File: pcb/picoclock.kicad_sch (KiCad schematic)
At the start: 62 parts, among them J1 UART, J10 USB, J11 Alt Power, J2 AUDIO, J3 xx, J4 xx, J5 Power In, J6 USB_C_Receptacle, J7 xx, J8 xx, J9 screen_adapter_connector, SW1 SW_Push, SW2 SW_Push, SW3 SW_Push, SW4 SW_Push, SW5 SW_Push, SW6 SW_Push, U1 PCF8563T, U2 Pico, U3 MCP9808_MSOP, U4 PCM5100, Y1 Crystal

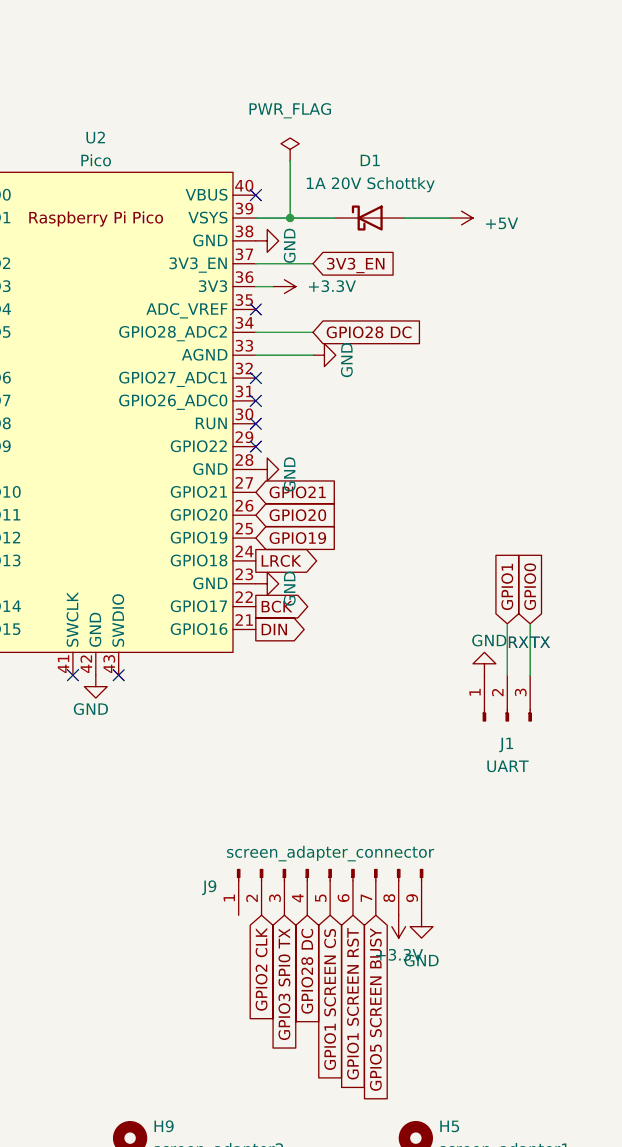
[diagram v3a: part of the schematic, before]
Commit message: [pcb] add PWR from epaper hat
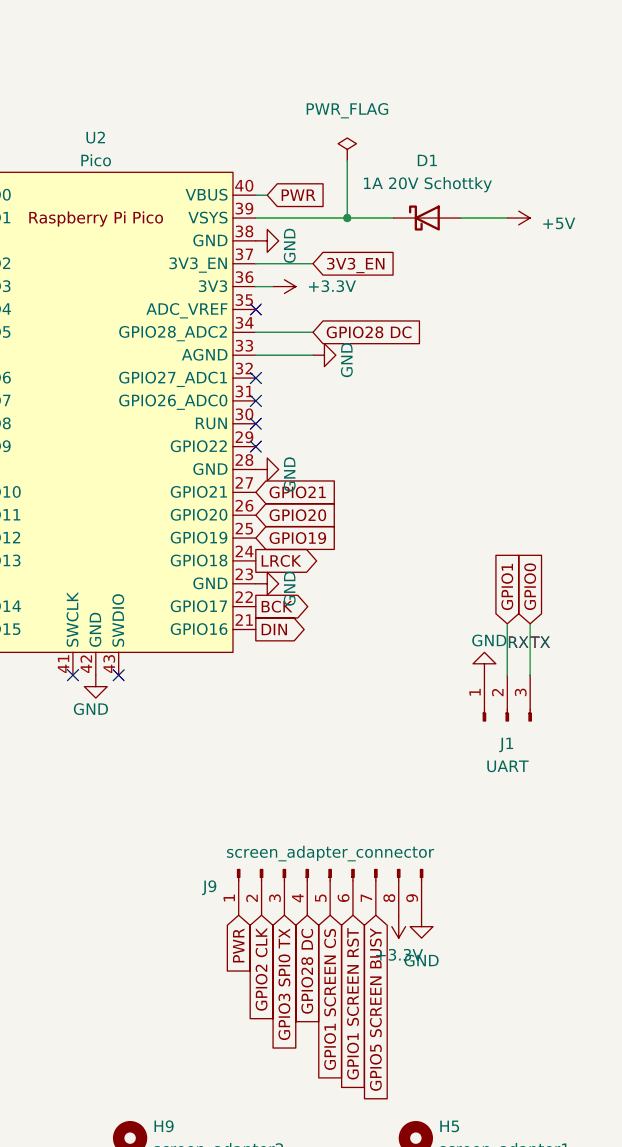
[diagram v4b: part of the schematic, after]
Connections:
- net PWR: now reaches J9.1 (Pin_1)
- net PWR: now also U2.40 (VBUS)
- no-connect marks 10 -> 9
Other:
- moved on the sheet: D1
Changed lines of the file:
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@@
   (junction (at 136.525 115.57) (diameter 0) (color 0 0 0 0)
   )
-  (junction (at 243.84 40.64) (diameter 0) (color 0 0 0 0)
-  )
   (junction (at 46.99 161.29) (diameter 0) (color 0 0 0 0)
   )
@@
   (junction (at 107.95 160.02) (diameter 0) (color 0 0 0 0)
   )
+  (junction (at 250.19 40.64) (diameter 0) (color 0 0 0 0)
+  )
   (junction (at 37.465 171.45) (diameter 0) (color 0 0 0 0)
   )
@@
   (no_connect (at 240.03 50.8))
   (no_connect (at 240.03 63.5))
-  (no_connect (at 240.03 38.1))
   (no_connect (at 204.47 86.36))
   (no_connect (at 240.03 60.96))
@@
     (stroke (width 0) (type default))
   )
-  (wire (pts (xy 256.54 40.64) (xy 261.62 40.64))
+  (wire (pts (xy 262.89 40.64) (xy 267.97 40.64))
     (stroke (width 0) (type default))
   )
@@
     (stroke (width 0) (type default))
   )
+  (wire (pts (xy 240.03 40.64) (xy 250.19 40.64))
+    (stroke (width 0) (type default))
+  )
   (polyline (pts (xy 15.875 148.59) (xy 15.875 192.405))
     (stroke (width 0) (type default))
@@
     (stroke (width 0) (type default))
   )
+  (wire (pts (xy 240.03 38.1) (xy 241.3 38.1))
+    (stroke (width 0) (type default))
+  )
   (wire (pts (xy 100.33 58.42) (xy 100.33 62.865))
     (stroke (width 0) (type default))
@@
     (stroke (width 0) (type default))
   )
-  (wire (pts (xy 243.84 34.29) (xy 243.84 40.64))
+  (wire (pts (xy 250.19 34.29) (xy 250.19 40.64))
     (stroke (width 0) (type default))
   )
@@
     (stroke (width 0) (type default))
   )
+  (wire (pts (xy 250.19 40.64) (xy 255.27 40.64))
+    (stroke (width 0) (type default))
+  )
   (wire (pts (xy 45.085 132.715) (xy 45.085 137.795))
     (stroke (width 0) (type default))
@@
     (stroke (width 0) (type default))
   )
-  (wire (pts (xy 243.84 40.64) (xy 248.92 40.64))
-    (stroke (width 0) (type default))
-  )
   (wire (pts (xy 33.02 171.45) (xy 37.465 171.45))
     (stroke (width 0) (type default))
@@
     (stroke (width 0) (type default))
   )
-  (wire (pts (xy 240.03 40.64) (xy 243.84 40.64))
-    (stroke (width 0) (type default))
-  )
   (text "Internal Temperature" (at 17.78 144.78 0)
     (effects (font (size 1.27 1.27)) (justify left bottom))
@@
     )
   )
+  (global_label "PWR" (shape input) (at 241.3 38.1 0) (fields_autoplaced)
+    (effects (font (size 1.27 1.27)) (justify left))
+    (property "Intersheetrefs" "${INTERSHEET_REFS}" (at 248.2766 38.1 0)
+      (effects (font (size 1.27 1.27)) (justify left) hide)
+    )
+  )
   (global_label "GPIO11" (shape input) (at 158.75 33.655 270) (fields_autoplaced)
     (effects (font (size 1.27 1.27)) (justify right))
@@
     )
   )
+  (global_label "PWR" (shape input) (at 238.125 118.11 270) (fields_autoplaced)
+    (effects (font (size 1.27 1.27)) (justify right))
+    (property "Intersheetrefs" "${INTERSHEET_REFS}" (at 238.125 125.0866 90)
+      (effects (font (size 1.27 1.27)) (justify right) hide)
+    )
+  )
   (global_label "GPIO21" (shape input) (at 107.315 104.14 0) (fields_autoplaced)
     (effects (font (size 1.27 1.27)) (justify left))
@@
     )
   )
-  (symbol (lib_id "power:+5V") (at 261.62 40.64 270) (unit 1)
+  (symbol (lib_id "power:+5V") (at 267.97 40.64 270) (unit 1)
     (in_bom yes) (on_board yes) (dnp no) (fields_autoplaced)
-    (property "Reference" "#PWR017" (at 257.81 40.64 0)
+    (property "Reference" "#PWR017" (at 264.16 40.64 0)
       (effects (font (size 1.27 1.27)) hide)
     )
-    (property "Value" "+5V" (at 265.43 41.275 90)
+    (property "Value" "+5V" (at 271.78 41.275 90)
       (effects (font (size 1.27 1.27)) (justify left))
     )
-    (property "Footprint" "" (at 261.62 40.64 0)
+    (property "Footprint" "" (at 267.97 40.64 0)
       (effects (font (size 1.27 1.27)) hide)
     )
-    (property "Datasheet" "" (at 261.62 40.64 0)
+    (property "Datasheet" "" (at 267.97 40.64 0)
       (effects (font (size 1.27 1.27)) hide)
     )
@@
     )
   )
-  (symbol (lib_id "Device:D_Schottky") (at 252.73 40.64 0) (unit 1)
+  (symbol (lib_id "Device:D_Schottky") (at 259.08 40.64 0) (unit 1)
     (in_bom yes) (on_board yes) (dnp no)
-    (property "Reference" "D1" (at 252.73 34.29 0)
+    (property "Reference" "D1" (at 259.08 34.29 0)
       (effects (font (size 1.27 1.27)))
     )
-    (property "Value" "1A 20V Schottky" (at 252.73 36.83 0)
+    (property "Value" "1A 20V Schottky" (at 259.08 36.83 0)
       (effects (font (size 1.27 1.27)))
     )
-    (property "Footprint" "Diode_SMD:D_SOD-123F" (at 252.73 40.64 0)
+    (property "Footprint" "Diode_SMD:D_SOD-123F" (at 259.08 40.64 0)
       (effects (font (size 1.27 1.27)) hide)
     )
-    (property "Datasheet" "~" (at 252.73 40.64 0)
+    (property "Datasheet" "~" (at 259.08 40.64 0)
       (effects (font (size 1.27 1.27)) hide)
     )
-    (property "LCSC" "C169527" (at 252.73 40.64 0)
+    (property "LCSC" "C169527" (at 259.08 40.64 0)
       (effects (font (size 1.27 1.27)) hide)
     )
@@
     )
   )
-  (symbol (lib_id "power:PWR_FLAG") (at 243.84 34.29 0) (unit 1)
+  (symbol (lib_id "power:PWR_FLAG") (at 250.19 34.29 0) (unit 1)
     (in_bom yes) (on_board yes) (dnp no) (fields_autoplaced)
-    (property "Reference" "#FLG01" (at 243.84 32.385 0)
+    (property "Reference" "#FLG01" (at 250.19 32.385 0)
       (effects (font (size 1.27 1.27)) hide)
     )
-    (property "Value" "PWR_FLAG" (at 243.84 28.575 0)
+    (property "Value" "PWR_FLAG" (at 250.19 28.575 0)
       (effects (font (size 1.27 1.27)))
     )
-    (property "Footprint" "" (at 243.84 34.29 0)
+    (property "Footprint" "" (at 250.19 34.29 0)
       (effects (font (size 1.27 1.27)) hide)
     )
-    (property "Datasheet" "~" (at 243.84 34.29 0)
+    (property "Datasheet" "~" (at 250.19 34.29 0)
       (effects (font (size 1.27 1.27)) hide)
     )

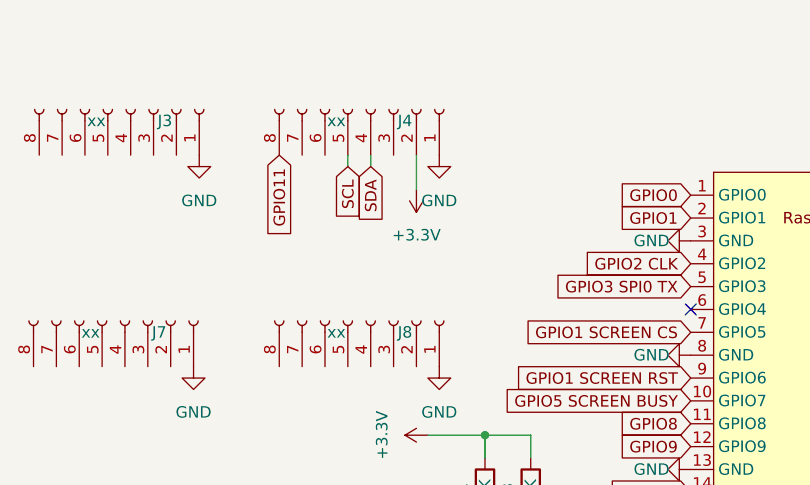
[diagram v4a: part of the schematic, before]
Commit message: [pcb] fix frontpanel pcb LEDs + connexion to main pcb
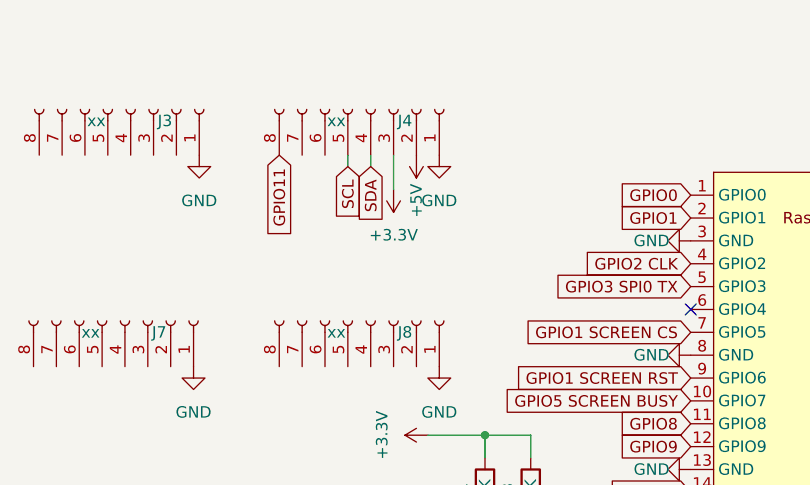
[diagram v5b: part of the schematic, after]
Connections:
- net +3.3V: now also J4.3 (Pin_3); no longer J4.2 (Pin_2)
- net +5V: now also J4.2 (Pin_2)
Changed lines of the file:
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@@
-    (stroke (width 0) (type default))
-  )
-  (wire (pts (xy 173.99 37.465) (xy 173.99 33.655))
     (stroke (width 0) (type default))
   )
@@
   )
   (wire (pts (xy 50.8 161.29) (xy 73.025 161.29))
+    (stroke (width 0) (type default))
+  )
+  (wire (pts (xy 171.45 37.465) (xy 171.45 33.655))
     (stroke (width 0) (type default))
   )
@@
     )
   )
+  (symbol (lib_id "power:+3.3V") (at 171.45 37.465 180) (unit 1)
+    (in_bom yes) (on_board yes) (dnp no)
+    (property "Reference" "#PWR048" (at 171.45 33.655 0)
+      (effects (font (size 1.27 1.27)) hide)
+    )
+    (property "Value" "+3.3V" (at 171.45 42.545 0)
+      (effects (font (size 1.27 1.27)))
+    )
+    (property "Footprint" "" (at 171.45 37.465 0)
+      (effects (font (size 1.27 1.27)) hide)
+    )
+    (property "Datasheet" "" (at 171.45 37.465 0)
+      (effects (font (size 1.27 1.27)) hide)
+    )
+    (pin "1")
+    (instances
+      (project "picoclock"
+        (path "/3b9dec0e-e0b7-4565-afc9-c4692f41aea9"
+          (reference "#PWR048") (unit 1)
+        )
+      )
+    )
+  )
   (symbol (lib_id "power:+3.3V") (at 136.525 120.015 270) (unit 1)
     (in_bom yes) (on_board yes) (dnp no)
@@
     )
   )
-  (symbol (lib_id "power:+3.3V") (at 173.99 37.465 180) (unit 1)
-    (in_bom yes) (on_board yes) (dnp no)
-    (property "Reference" "#PWR048" (at 173.99 33.655 0)
-      (effects (font (size 1.27 1.27)) hide)
-    )
-    (property "Value" "+3.3V" (at 173.99 42.545 0)
-      (effects (font (size 1.27 1.27)))
-    )
-    (property "Footprint" "" (at 173.99 37.465 0)
-      (effects (font (size 1.27 1.27)) hide)
-    )
-    (property "Datasheet" "" (at 173.99 37.465 0)
-      (effects (font (size 1.27 1.27)) hide)
-    )
-    (pin "1")
-    (instances
-      (project "picoclock"
-        (path "/3b9dec0e-e0b7-4565-afc9-c4692f41aea9"
-          (reference "#PWR048") (unit 1)
-        )
-      )
-    )
-  )
   (symbol (lib_id "power:+3.3V") (at 105.41 107.95 270) (unit 1)
     (in_bom yes) (on_board yes) (dnp no)
@@
         )
       )
+    )
+  )
+  (symbol (lib_id "power:+5V") (at 173.99 33.655 180) (unit 1)
+    (in_bom yes) (on_board yes) (dnp no)
+    (property "Reference" "#PWR070" (at 173.99 29.845 0)
+      (effects (font (size 1.27 1.27)) hide)
+    )
+    (property "Value" "+5V" (at 173.99 36.83 90)
+      (effects (font (size 1.27 1.27)) (justify left))
+    )
+    (property "Footprint" "" (at 173.99 33.655 0)
+      (effects (font (size 1.27 1.27)) hide)
+    )
+    (property "Datasheet" "" (at 173.99 33.655 0)
+      (effects (font (size 1.27 1.27)) hide)
+    )
+    (pin "1")
+    (instances
+      (project "picoclock"
+        (path "/3b9dec0e-e0b7-4565-afc9-c4692f41aea9"
+          (reference "#PWR070") (unit 1)
+        )
+      )

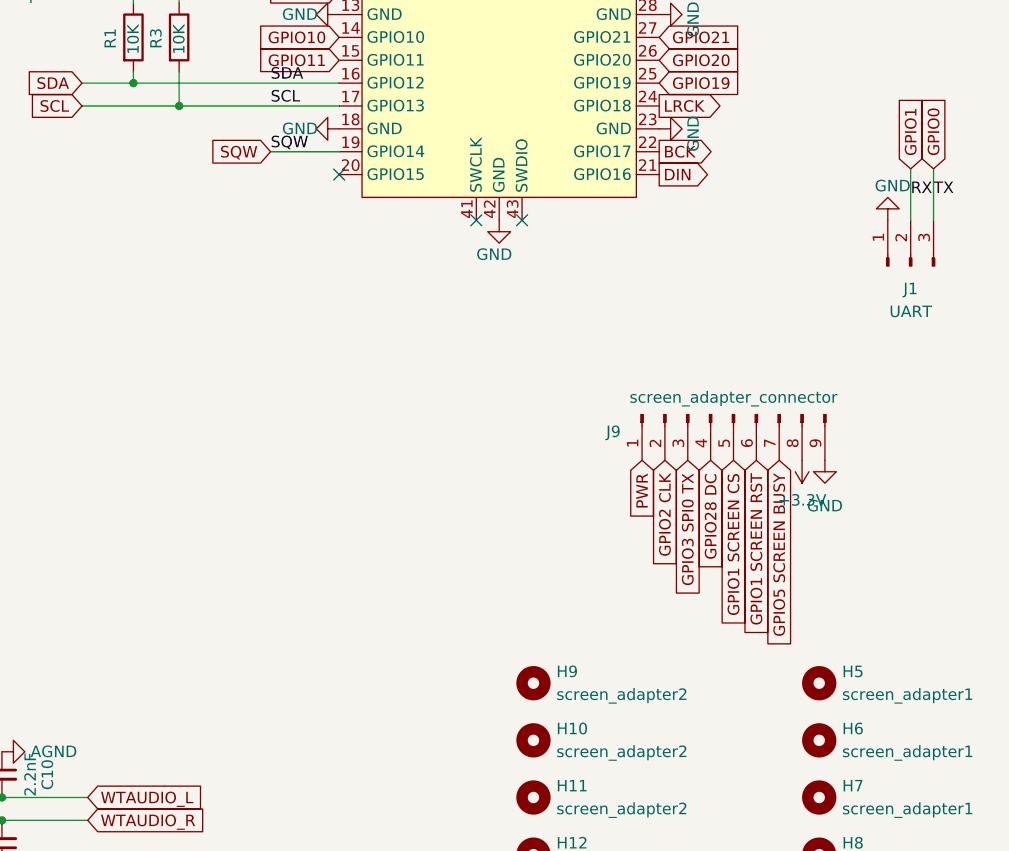
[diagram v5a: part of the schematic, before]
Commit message: [pcb] add PWM out
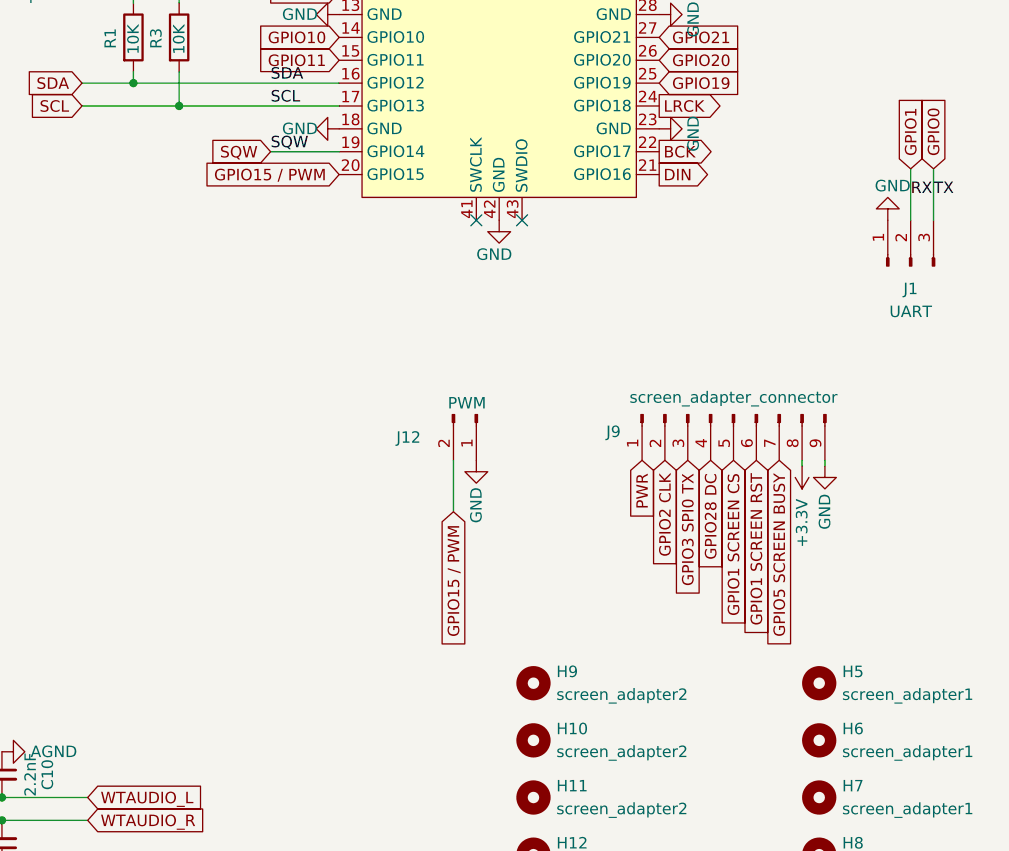
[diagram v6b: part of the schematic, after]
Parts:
- added J12: PWM, Connector_PinHeader_2.54mm:PinHeader_1x02_P2.54mm_Vertical, symbol Connector:Conn_01x02_Pin
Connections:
- net GND: now also J12.1 (Pin_1)
- net GPIO15 / PWM: now reaches U2.20 (GPIO15)
- net GPIO15 / PWM: now also J12.2 (Pin_2)
- no-connect marks 9 -> 8
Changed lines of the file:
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@@
   (no_connect (at 240.03 50.8))
   (no_connect (at 240.03 63.5))
-  (no_connect (at 204.47 86.36))
   (no_connect (at 240.03 60.96))
   (no_connect (at 204.47 50.8))
@@
     (stroke (width 0) (type default))
   )
+  (wire (pts (xy 217.17 123.825) (xy 217.17 118.11))
+    (stroke (width 0) (type default))
+  )
   (polyline (pts (xy 15.875 192.405) (xy 87.63 192.405))
     (stroke (width 0) (type default))
@@
     (stroke (width 0) (type default))
   )
+  (wire (pts (xy 255.905 118.745) (xy 255.905 118.11))
+    (stroke (width 0) (type default))
+  )
   (wire (pts (xy 33.02 48.26) (xy 35.56 48.26))
     (stroke (width 0) (type default))
@@
     (stroke (width 0) (type default))
   )
+  (wire (pts (xy 258.445 118.745) (xy 258.445 118.11))
+    (stroke (width 0) (type default))
+  )
   (wire (pts (xy 105.41 47.625) (xy 105.41 56.515))
     (stroke (width 0) (type default))
@@
     )
   )
+  (global_label "GPIO15 {slash} PWM" (shape input) (at 204.47 86.36 180) (fields_autoplaced)
+    (effects (font (size 1.27 1.27)) (justify right))
+    (property "Intersheetrefs" "${INTERSHEET_REFS}" (at 187.152 86.36 0)
+      (effects (font (size 1.27 1.27)) (justify right) hide)
+    )
+  )
   (global_label "GPIO0" (shape input) (at 204.47 38.1 180) (fields_autoplaced)
     (effects (font (size 1.27 1.27)) (justify right))
@@
     )
   )
+  (global_label "GPIO15 {slash} PWM" (shape input) (at 217.17 123.825 270) (fields_autoplaced)
+    (effects (font (size 1.27 1.27)) (justify right))
+    (property "Intersheetrefs" "${INTERSHEET_REFS}" (at 217.17 141.143 90)
+      (effects (font (size 1.27 1.27)) (justify right) hide)
+    )
+  )
   (global_label "LRCK" (shape output) (at 240.03 78.74 0) (fields_autoplaced)
     (effects (font (size 1.27 1.27)) (justify left))
@@
     )
   )
-  (symbol (lib_id "power:+3.3V") (at 255.905 118.11 180) (unit 1)
-    (in_bom yes) (on_board yes) (dnp no) (fields_autoplaced)
-    (property "Reference" "#PWR01" (at 255.905 114.3 0)
+  (symbol (lib_id "power:+3.3V") (at 255.905 118.745 180) (unit 1)
+    (in_bom yes) (on_board yes) (dnp no)
+    (property "Reference" "#PWR01" (at 255.905 114.935 0)
       (effects (font (size 1.27 1.27)) hide)
     )
-    (property "Value" "+3.3V" (at 255.905 122.555 0)
+    (property "Value" "+3.3V" (at 255.905 125.095 90)
       (effects (font (size 1.27 1.27)))
     )
-    (property "Footprint" "" (at 255.905 118.11 0)
+    (property "Footprint" "" (at 255.905 118.745 0)
       (effects (font (size 1.27 1.27)) hide)
     )
-    (property "Datasheet" "" (at 255.905 118.11 0)
+    (property "Datasheet" "" (at 255.905 118.745 0)
       (effects (font (size 1.27 1.27)) hide)
     )
@@
     )
   )
+  (symbol (lib_id "power:GND") (at 219.71 118.11 0) (unit 1)
+    (in_bom yes) (on_board yes) (dnp no)
+    (property "Reference" "#PWR072" (at 219.71 124.46 0)
+      (effects (font (size 1.27 1.27)) hide)
+    )
+    (property "Value" "GND" (at 219.71 125.095 90)
+      (effects (font (size 1.27 1.27)) (justify left))
+    )
+    (property "Footprint" "" (at 219.71 118.11 0)
+      (effects (font (size 1.27 1.27)) hide)
+    )
+    (property "Datasheet" "" (at 219.71 118.11 0)
+      (effects (font (size 1.27 1.27)) hide)
+    )
+    (pin "1")
+    (instances
+      (project "picoclock"
+        (path "/3b9dec0e-e0b7-4565-afc9-c4692f41aea9"
+          (reference "#PWR072") (unit 1)
+        )
+      )
+    )
+  )
   (symbol (lib_id "Device:C_Small") (at 99.06 157.48 180) (unit 1)
     (in_bom yes) (on_board yes) (dnp no)
@@
     )
   )
+  (symbol (lib_id "Connector:Conn_01x02_Pin") (at 219.71 113.03 270) (unit 1)
+    (in_bom yes) (on_board yes) (dnp no)
+    (property "Reference" "J12" (at 210.82 115.57 90)
+      (effects (font (size 1.27 1.27)) (justify left))
+    )
+    (property "Value" "PWM" (at 216.535 111.76 90)
+      (effects (font (size 1.27 1.27)) (justify left))
+    )
+    (property "Footprint" "Connector_PinHeader_2.54mm:PinHeader_1x02_P2.54mm_Vertical" (at 219.71 113.03 0)
+      (effects (font (size 1.27 1.27)) hide)
+    )
+    (property "Datasheet" "~" (at 219.71 113.03 0)
+      (effects (font (size 1.27 1.27)) hide)
+    )
+    (pin "1")
+    (pin "2")
+    (instances
+      (project "picoclock"
+        (path "/3b9dec0e-e0b7-4565-afc9-c4692f41aea9"
+          (reference "J12") (unit 1)
+        )
+      )
+    )
+  )
   (symbol (lib_id "Connector:Conn_01x08_Socket") (at 142.24 28.575 270) (mirror x) (unit 1)
     (in_bom yes) (on_board yes) (dnp no)
@@
     )
   )
-  (symbol (lib_id "power:GND") (at 258.445 118.11 0) (unit 1)
-    (in_bom yes) (on_board yes) (dnp no) (fields_autoplaced)
-    (property "Reference" "#PWR053" (at 258.445 124.46 0)
+  (symbol (lib_id "power:GND") (at 258.445 118.745 0) (unit 1)
+    (in_bom yes) (on_board yes) (dnp no)
+    (property "Reference" "#PWR053" (at 258.445 125.095 0)
       (effects (font (size 1.27 1.27)) hide)
     )
-    (property "Value" "GND" (at 258.445 123.19 0)
+    (property "Value" "GND" (at 258.445 123.825 90)
       (effects (font (size 1.27 1.27)))
     )
-    (property "Footprint" "" (at 258.445 118.11 0)
+    (property "Footprint" "" (at 258.445 118.745 0)
       (effects (font (size 1.27 1.27)) hide)
     )
-    (property "Datasheet" "" (at 258.445 118.11 0)
+    (property "Datasheet" "" (at 258.445 118.745 0)
       (effects (font (size 1.27 1.27)) hide)
     )
